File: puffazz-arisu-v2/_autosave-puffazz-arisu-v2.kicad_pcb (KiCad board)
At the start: 2 copper layers, 339.1 x 118.7 mm, 82 parts, among them SW1 SW_Push, U1 ATmega32U4-AU, Y1 16MHz

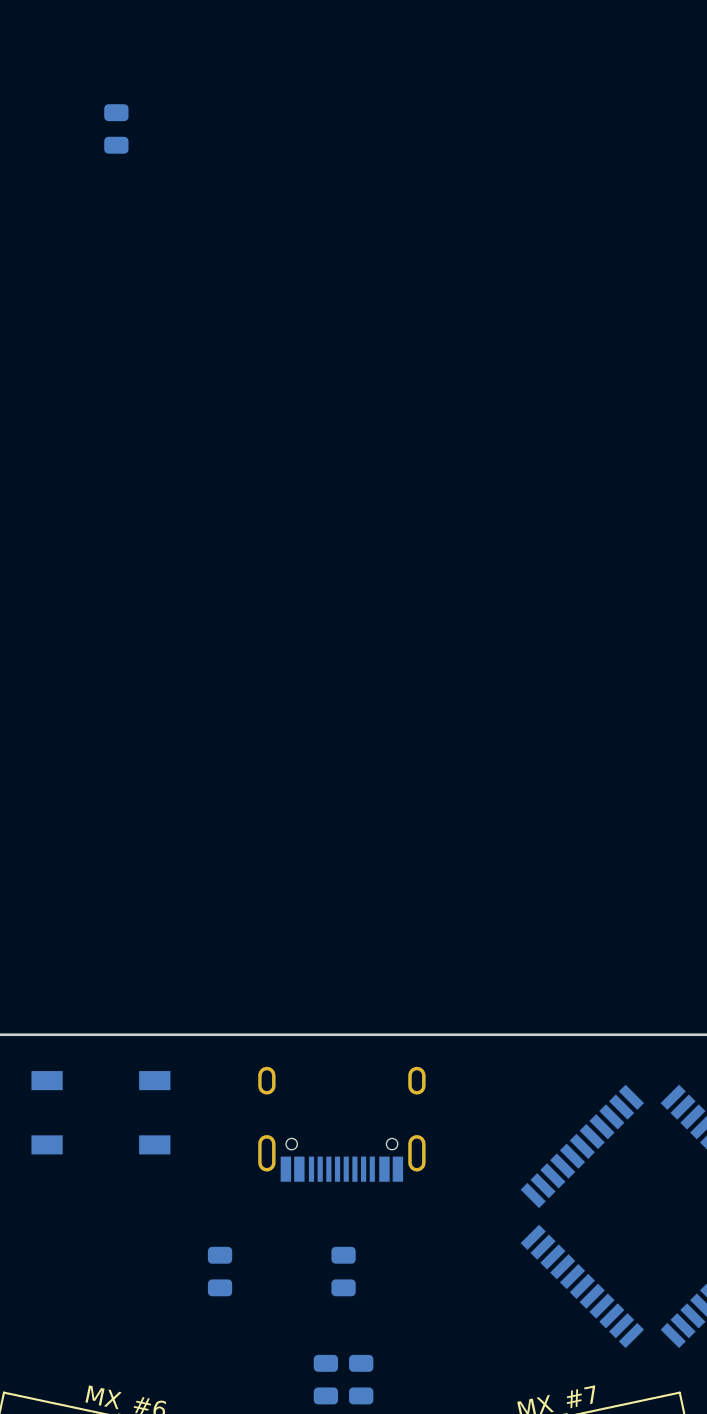
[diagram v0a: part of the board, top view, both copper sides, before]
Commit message: Finished routing switches and RGB LED
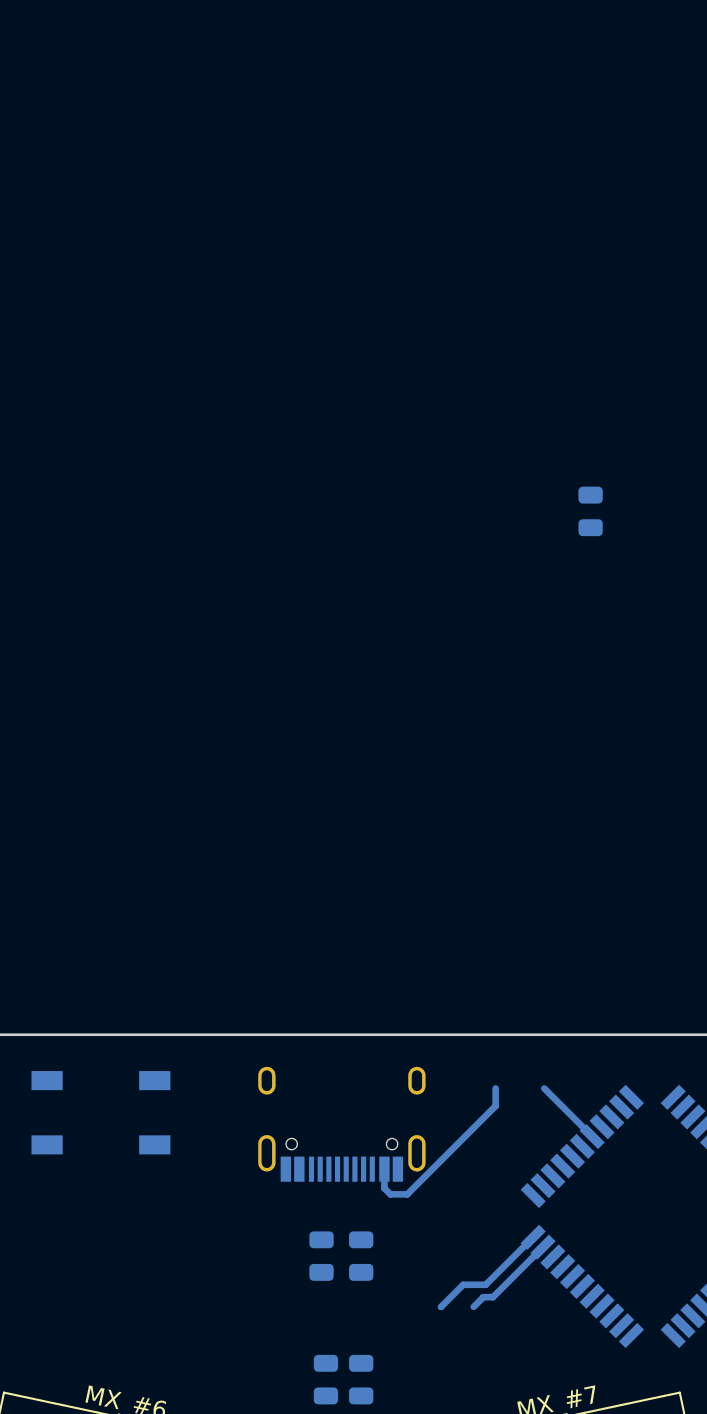
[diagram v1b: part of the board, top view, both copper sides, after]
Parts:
- moved R1 35.1 mm to (199.6, 20.1)
- moved R6 5.91 mm to (184.2, 63.0)
- moved R5 1.35 mm to (186.4, 63.0)
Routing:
- net +5V: track 848.0 -> 858.8 mm
- net VCC: track 0.00 -> 10.8 mm
- net GND: track 810.9 -> 816.3 mm
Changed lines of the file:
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@@
     (thickness 1.6)
     (drawings 1398)
-    (tracks 1141)
+    (tracks 1157)
     (zones 0)
     (modules 185)
@@
   )
   (module Resistor_SMD:R_0805_2012Metric (layer B.Cu)
-    (at 178.308 63.881 270)
+    (at 184.15 62.992 270)
     (descr "Resistor SMD 0805 (2012 Metric), square (rectangular) end terminal, IPC_7351 nominal, (Body size source: https://docs.google.com/spreadsheets/d/1BsfQQcO9C6DZCsRaXUlFlo91Tg2WpOkGARC1WS5S8t0/edit?usp=sharing), generated with kicad-footprint-generator")
     (tags resistor)
@@
   )
   (module Resistor_SMD:R_0805_2012Metric (layer B.Cu)
-    (at 185.42 63.881 270)
+    (at 186.436 62.992 270)
     (descr "Resistor SMD 0805 (2012 Metric), square (rectangular) end terminal, IPC_7351 nominal, (Body size source: https://docs.google.com/spreadsheets/d/1BsfQQcO9C6DZCsRaXUlFlo91Tg2WpOkGARC1WS5S8t0/edit?usp=sharing), generated with kicad-footprint-generator")
     (tags resistor)
@@
   )
   (module Resistor_SMD:R_0805_2012Metric (layer B.Cu)
-    (at 172.339 -1.905 90)
+    (at 199.644 20.1145 90)
     (descr "Resistor SMD 0805 (2012 Metric), square (rectangular) end terminal, IPC_7351 nominal, (Body size source: https://docs.google.com/spreadsheets/d/1BsfQQcO9C6DZCsRaXUlFlo91Tg2WpOkGARC1WS5S8t0/edit?usp=sharing), generated with kicad-footprint-generator")
     (tags resistor)
@@
   )
   (module Fuse:Fuse_1206_3216Metric (layer B.Cu)
-    (at 188.595 64.519 90)
+    (at 195.577 53.34 180)
     (descr "Fuse SMD 1206 (3216 Metric), square (rectangular) end terminal, IPC_7351 nominal, (Body size source: http://www.tortai-tech.com/upload/download/2011102023233369053.pdf), generated with kicad-footprint-generator")
     (tags resistor)
     (attr smd)
-    (fp_text reference F1 (at 0 1.82 270) (layer B.SilkS)
+    (fp_text reference F1 (at 0 1.82 180) (layer B.SilkS)
       (effects (font (size 1 1) (thickness 0.15)) (justify mirror))
     )
-    (fp_text value 500mA (at 0 -1.82 270) (layer B.Fab)
+    (fp_text value 500mA (at 0 -1.82 180) (layer B.Fab)
       (effects (font (size 1 1) (thickness 0.15)) (justify mirror))
     )
-    (fp_text user %R (at 0 0 270) (layer B.Fab)
+    (fp_text user %R (at 0 0 180) (layer B.Fab)
       (effects (font (size 0.8 0.8) (thickness 0.12)) (justify mirror))
     )
@@
     (fp_line (start 2.28 1.12) (end 2.28 -1.12) (layer B.CrtYd) (width 0.05))
     (fp_line (start 2.28 -1.12) (end -2.28 -1.12) (layer B.CrtYd) (width 0.05))
-    (pad 2 smd roundrect (at 1.4 0 90) (size 1.25 1.75) (layers B.Cu B.Paste B.Mask) (roundrect_rratio 0.2)
+    (pad 2 smd roundrect (at 1.4 0 180) (size 1.25 1.75) (layers B.Cu B.Paste B.Mask) (roundrect_rratio 0.2)
       (net 6 VCC))
-    (pad 1 smd roundrect (at -1.4 0 90) (size 1.25 1.75) (layers B.Cu B.Paste B.Mask) (roundrect_rratio 0.2)
+    (pad 1 smd roundrect (at -1.4 0 180) (size 1.25 1.75) (layers B.Cu B.Paste B.Mask) (roundrect_rratio 0.2)
       (net 5 +5V))
     (model ${KISYS3DMOD}/Fuse.3dshapes/Fuse_1206_3216Metric.wrl
@@
   )
   (module Package_TO_SOT_SMD:SOT-143 (layer B.Cu)
-    (at 181.864 63.881 180)
+    (at 181.745 63.33 270)
     (descr SOT-143)
     (tags SOT-143)
     (attr smd)
-    (fp_text reference D1 (at 0.02 2.38) (layer B.SilkS)
+    (fp_text reference D1 (at 0.02 2.38 90) (layer B.SilkS)
       (effects (font (size 1 1) (thickness 0.15)) (justify mirror))
     )
-    (fp_text value PRTR5V0U2X (at -0.28 -2.48) (layer B.Fab)
+    (fp_text value PRTR5V0U2X (at -0.28 -2.48 90) (layer B.Fab)
       (effects (font (size 1 1) (thickness 0.15)) (justify mirror))
     )
-    (fp_text user %R (at 0 0 270) (layer B.Fab)
+    (fp_text user %R (at 0 0 180) (layer B.Fab)
       (effects (font (size 0.5 0.5) (thickness 0.075)) (justify mirror))
     )
@@
     (fp_line (start -2.05 -1.75) (end 2.05 -1.75) (layer B.CrtYd) (width 0.05))
     (fp_line (start -2.05 -1.75) (end -2.05 1.75) (layer B.CrtYd) (width 0.05))
-    (pad 4 smd rect (at 1.1 0.95 270) (size 1 1.4) (layers B.Cu B.Paste B.Mask)
+    (pad 4 smd rect (at 1.1 0.95) (size 1 1.4) (layers B.Cu B.Paste B.Mask)
       (net 6 VCC))
-    (pad 3 smd rect (at 1.1 -0.95 270) (size 1 1.4) (layers B.Cu B.Paste B.Mask)
+    (pad 3 smd rect (at 1.1 -0.95) (size 1 1.4) (layers B.Cu B.Paste B.Mask)
       (net 7 "Net-(D1-Pad3)"))
-    (pad 2 smd rect (at -1.1 -0.95 270) (size 1 1.4) (layers B.Cu B.Paste B.Mask)
+    (pad 2 smd rect (at -1.1 -0.95) (size 1 1.4) (layers B.Cu B.Paste B.Mask)
       (net 8 "Net-(D1-Pad2)"))
-    (pad 1 smd rect (at -1.1 0.77 270) (size 1.2 1.4) (layers B.Cu B.Paste B.Mask)
+    (pad 1 smd rect (at -1.1 0.77) (size 1.2 1.4) (layers B.Cu B.Paste B.Mask)
       (net 1 GND))
     (model ${KISYS3DMOD}/Package_TO_SOT_SMD.3dshapes/SOT-143.wrl
@@
   )
   (module Capacitor_SMD:C_0805_2012Metric (layer B.Cu)
-    (at 200.533 -1.905 90)
+    (at 191.9755 65.913)
     (descr "Capacitor SMD 0805 (2012 Metric), square (rectangular) end terminal, IPC_7351 nominal, (Body size source: https://docs.google.com/spreadsheets/d/1BsfQQcO9C6DZCsRaXUlFlo91Tg2WpOkGARC1WS5S8t0/edit?usp=sharing), generated with kicad-footprint-generator")
     (tags capacitor)
     (attr smd)
-    (fp_text reference C6 (at 0 1.65 270) (layer B.SilkS)
+    (fp_text reference C6 (at 0 1.65 180) (layer B.SilkS)
       (effects (font (size 1 1) (thickness 0.15)) (justify mirror))
     )
-    (fp_text value 0.1uF (at 0 -1.65 270) (layer B.Fab)
+    (fp_text value 0.1uF (at 0 -1.65 180) (layer B.Fab)
       (effects (font (size 1 1) (thickness 0.15)) (justify mirror))
     )
-    (fp_text user %R (at 0 0 270) (layer B.Fab)
+    (fp_text user %R (at 0 0 180) (layer B.Fab)
       (effects (font (size 0.5 0.5) (thickness 0.08)) (justify mirror))
     )
@@
     (fp_line (start 1.68 0.95) (end 1.68 -0.95) (layer B.CrtYd) (width 0.05))
     (fp_line (start 1.68 -0.95) (end -1.68 -0.95) (layer B.CrtYd) (width 0.05))
-    (pad 2 smd roundrect (at 0.9375 0 90) (size 0.975 1.4) (layers B.Cu B.Paste B.Mask) (roundrect_rratio 0.25)
+    (pad 2 smd roundrect (at 0.9375 0) (size 0.975 1.4) (layers B.Cu B.Paste B.Mask) (roundrect_rratio 0.25)
       (net 1 GND))
-    (pad 1 smd roundrect (at -0.9375 0 90) (size 0.975 1.4) (layers B.Cu B.Paste B.Mask) (roundrect_rratio 0.25)
+    (pad 1 smd roundrect (at -0.9375 0) (size 0.975 1.4) (layers B.Cu B.Paste B.Mask) (roundrect_rratio 0.25)
       (net 5 +5V))
     (model ${KISYS3DMOD}/Capacitor_SMD.3dshapes/C_0805_2012Metric.wrl
@@
   (segment (start 147.613 54.864) (end 147.664 54.813) (width 0.38) (layer B.Cu) (net 1))
   (segment (start 144.907 54.864) (end 147.613 54.864) (width 0.38) (layer B.Cu) (net 1))
+  (segment (start 196.30571 63.074807) (end 196.90675 62.473767) (width 0.38) (layer B.Cu) (net 1))
+  (segment (start 194.023754 65.356763) (end 196.30571 63.074807) (width 0.38) (layer B.Cu) (net 1))
+  (segment (start 193.469237 65.356763) (end 194.023754 65.356763) (width 0.38) (layer B.Cu) (net 1))
+  (segment (start 192.913 65.913) (end 193.469237 65.356763) (width 0.38) (layer B.Cu) (net 1))
   (segment (start 36.627 82.6155) (end 36.627 82.982) (width 0.38) (layer B.Cu) (net 5))
   (segment (start 37.9245 81.318) (end 36.627 82.6155) (width 0.38) (layer B.Cu) (net 5))
@@
   (segment (start 144.907 52.4015) (end 146.585501 50.722999) (width 0.38) (layer B.Cu) (net 5))
   (segment (start 144.907 52.989) (end 144.907 52.4015) (width 0.38) (layer B.Cu) (net 5))
+  (segment (start 191.032 65.919) (end 191.038 65.913) (width 0.38) (layer B.Cu) (net 5))
+  (segment (start 196.341064 61.908082) (end 193.606146 64.643) (width 0.38) (layer B.Cu) (net 5))
+  (segment (start 192.308 64.643) (end 191.038 65.913) (width 0.38) (layer B.Cu) (net 5))
+  (segment (start 193.606146 64.643) (end 192.308 64.643) (width 0.38) (layer B.Cu) (net 5))
+  (segment (start 199.735177 56.098177) (end 199.735177 56.109806) (width 0.38) (layer B.Cu) (net 5))
+  (segment (start 196.977 53.34) (end 199.735177 56.098177) (width 0.38) (layer B.Cu) (net 5))
+  (segment (start 187.774 59.092) (end 188.118 59.436) (width 0.38) (layer B.Cu) (net 6))
+  (segment (start 187.774 57.987) (end 187.774 59.092) (width 0.38) (layer B.Cu) (net 6))
+  (segment (start 194.177 54.315) (end 194.177 53.34) (width 0.38) (layer B.Cu) (net 6))
+  (segment (start 194.177 54.347664) (end 194.177 54.315) (width 0.38) (layer B.Cu) (net 6))
+  (segment (start 189.088664 59.436) (end 194.177 54.347664) (width 0.38) (layer B.Cu) (net 6))
+  (segment (start 188.118 59.436) (end 189.088664 59.436) (width 0.38) (layer B.Cu) (net 6))
   (segment (start 54.895707 61.992918) (end 53.340073 61.992918) (width 0.25) (layer B.Cu) (net 9))
   (segment (start 57.992918 61.992918) (end 54.895707 61.992918) (width 0.25) (layer B.Cu) (net 9))
